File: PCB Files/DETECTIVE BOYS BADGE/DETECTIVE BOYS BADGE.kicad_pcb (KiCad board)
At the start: 2 copper layers, 45.9 x 55 mm, 40 parts, among them J1 Jack 3.5mm, SW1 SPDT_PCM12, SW2 Pushbutton, U1 NRF24L01_Breakout, U2 MIC5205-3.3YM5, U3 TP4056, U4 LM358, U5 ATmega328P-A, X1 Resonator 8MHz

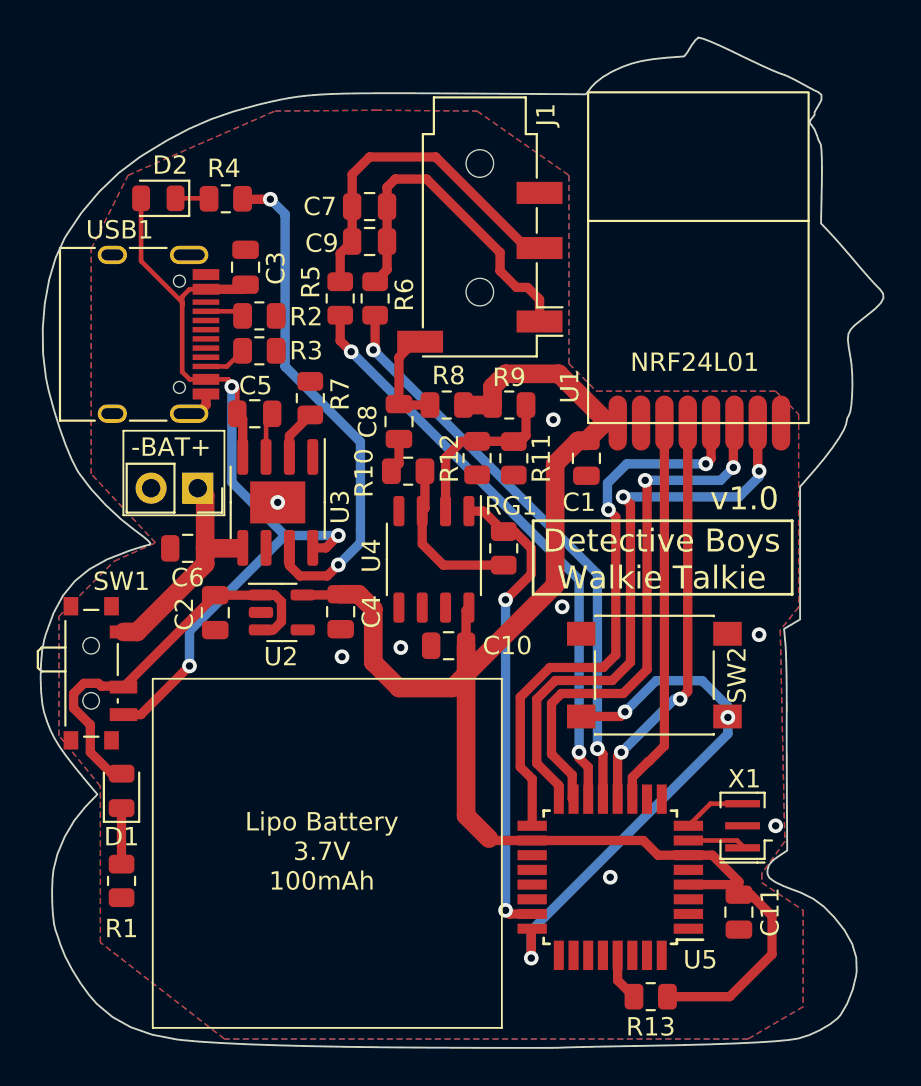
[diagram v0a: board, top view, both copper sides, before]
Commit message: Updated PCB version to v1.1
Fixed some schematic error designs at audio amplifier circuit, modified NRF24 mini footprint to easier placement.
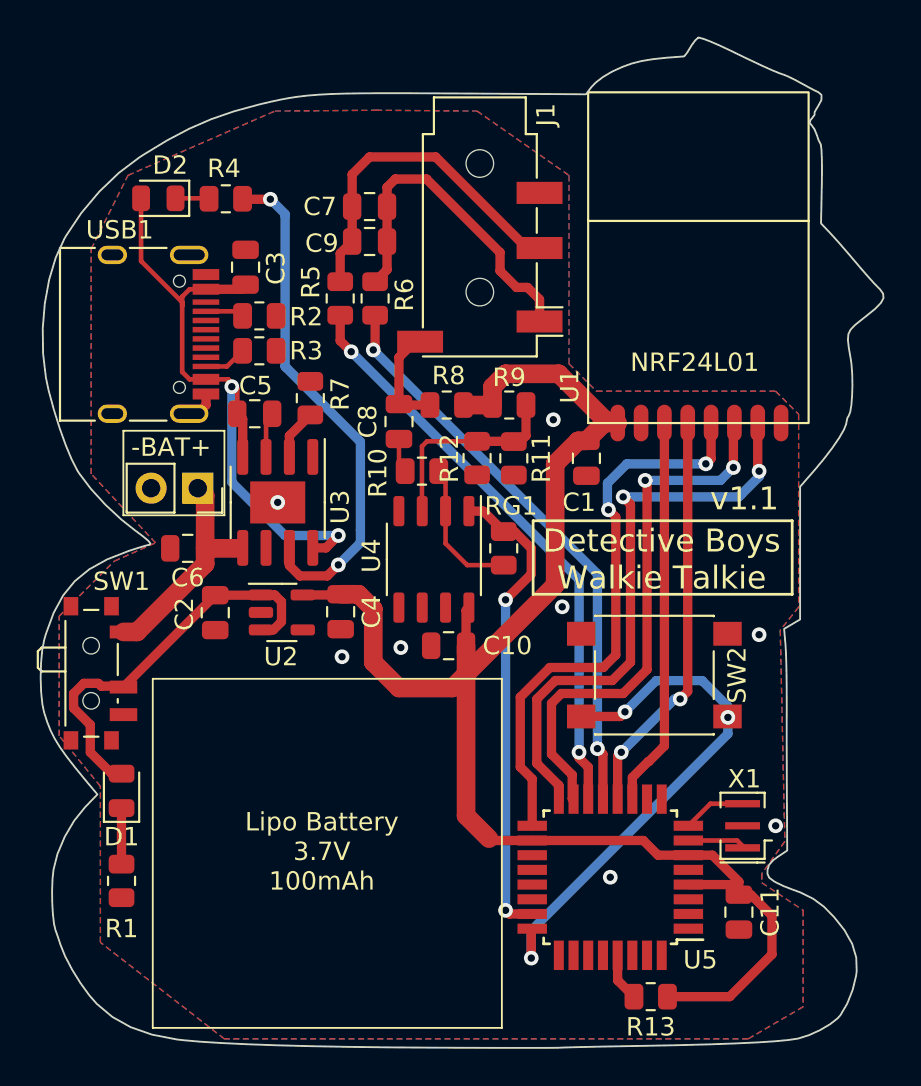
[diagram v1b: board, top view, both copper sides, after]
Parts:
- C7, C9: value 100nF -> 330nF
- C8: value 1uF -> 10uF
- moved R10 0.75 mm to (151.2, 123.6)
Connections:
- BT1 pad 1: BAT -> /BAT
- C6 pad 1: BAT -> /BAT
- SW1 pad 1: BAT -> VBAT
- SW1 pad 3: VBUS -> unconnected-(SW1-Pad3)
- U3 pad 5: BAT -> /BAT
- U4 pad 2: Net-(R11-Pad2) -> Net-(R10-Pad1)
- U4 pad 3: Net-(R10-Pad1) -> Net-(R11-Pad2)
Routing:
- net VBUS: track 49.6 -> 35.7 mm, vias 3 -> 2
- net BAT: track 12.0 -> 0.00 mm
- net /BAT: track 0.00 -> 12.0 mm
- net Net-(R11-Pad2): track 9.47 -> 10.8 mm
- net Net-(R10-Pad1): track 8.94 -> 7.74 mm
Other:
- board text added: "v1.1"
- board text removed: "v1.0"

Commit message: Updated PCB (v1.2)
Added a flexPCB connector on the edge of the board connected to the ICSP pins, making easier to program the ATMEGA328P.
The battery terminals footprint is now only on one side of the board, preventing accidental short-circuit on the bottom side.
Moved some components to allow more space for the LiPo battery.
Changed the values of components C7,C9 R5,R6, adjusting the values for filtering the audio output.
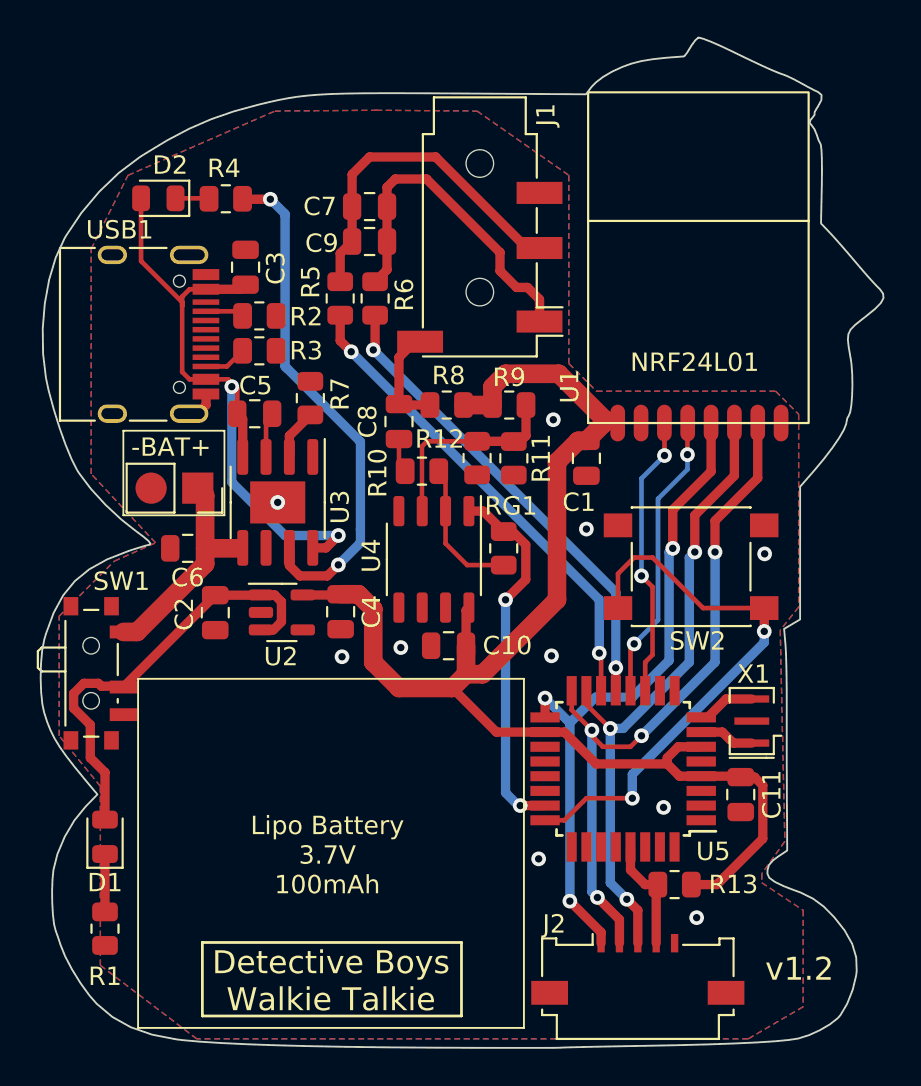
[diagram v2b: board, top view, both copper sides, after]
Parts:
- added J2: ICSP, Connector_FFC-FPC:Molex_200528-0050_1x05-1MP_P1.00mm_Horizontal, F.Cu at (163.0, 150.2)
- moved C11 6.40 mm to (168.6, 141.2)
- moved R13 6.24 mm to (165.0, 146.1)
- moved SW2 6.23 mm to (165.9, 128.8)
- moved U5 5.94 mm to (162.2, 139.8)
- moved X1 5.72 mm to (169.2, 137.2)
- moved R1 2.75 mm to (134.0, 148.5)
- moved D1 2.66 mm to (134.0, 143.5)
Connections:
- BT1 pad 1: /BAT -> BAT
- C6 pad 1: /BAT -> BAT
- SW1 pad 1: VBAT -> BAT
- U3 pad 5: /BAT -> BAT
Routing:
- net BAT: track 0.00 -> 12.0 mm
- net /BAT: track 12.0 -> 0.00 mm
- net +3V3: track 83.4 -> 73.8 mm
- net CSN: track 22.2 -> 15.9 mm
- net MISO: track 31.8 -> 38.0 mm, vias 2 -> 4
- net A0: track 26.0 -> 20.2 mm
- net CE: track 21.2 -> 15.5 mm, vias 0 -> 2
- net AUDIO_R: track 31.9 -> 26.3 mm
- net AUDIO_L: track 31.6 -> 26.1 mm
- net SCK: track 31.1 -> 36.3 mm, vias 2 -> 3
- net MOSI: track 29.6 -> 34.8 mm, vias 2 -> 3
- net RESET: track 2.62 -> 6.30 mm
- net /VIN: track 22.0 -> 23.8 mm
- net A1: track 29.1 -> 29.9 mm, vias 3 -> 2
- net GND: vias 8 -> 10
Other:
- board text added: "v1.2"
- board text removed: "v1.1"
